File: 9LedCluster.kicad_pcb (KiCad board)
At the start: 4 copper layers, 26 x 26 mm, 43 parts, among them J1 Input, J2 Output, U1 LMR54406DBVR, U2 TLC5971RGE

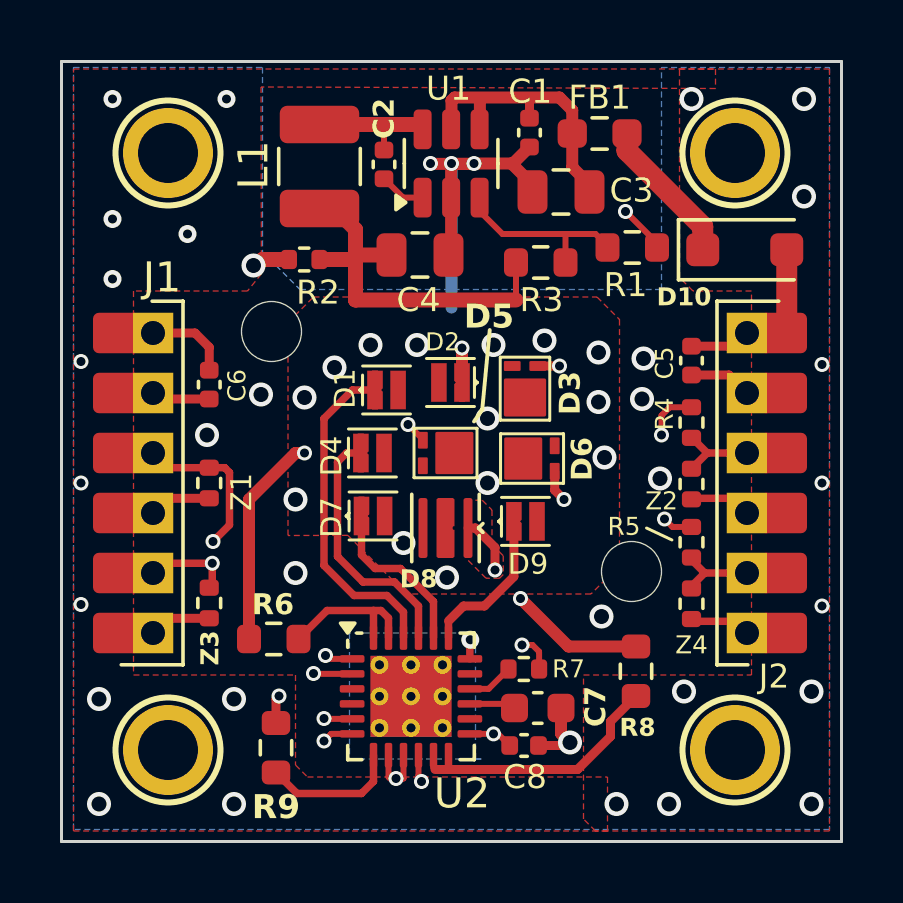
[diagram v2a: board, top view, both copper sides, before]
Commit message: Fix center ref for CREE LEDs for 9LED.
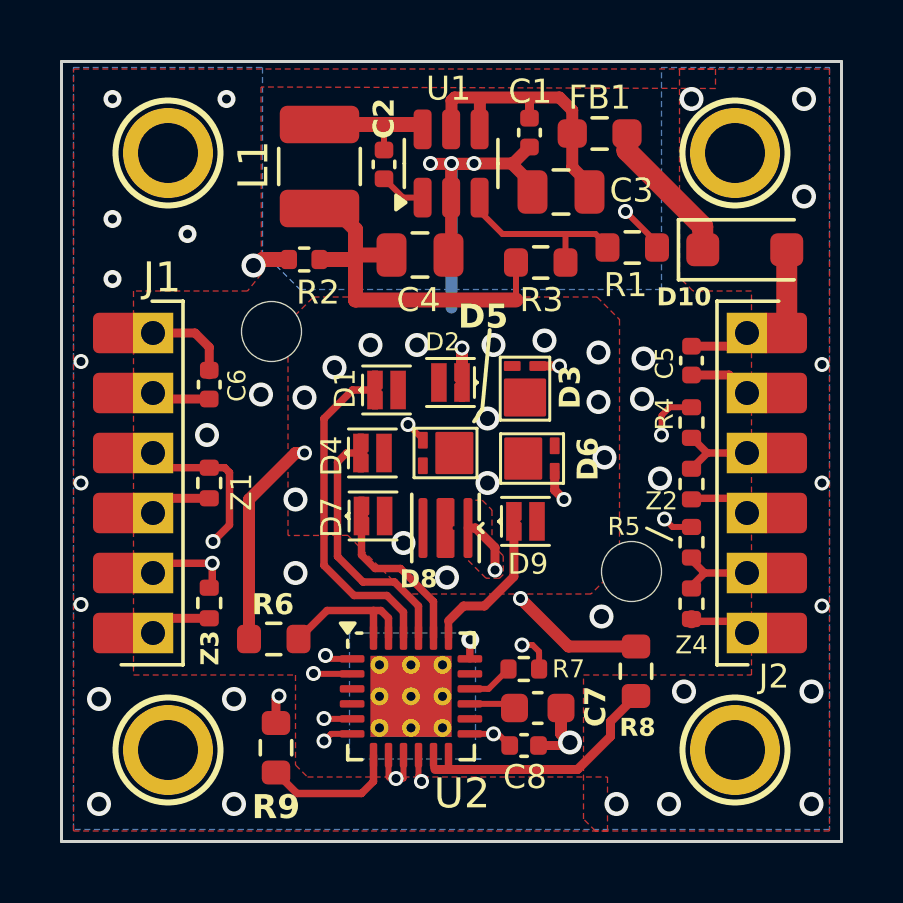
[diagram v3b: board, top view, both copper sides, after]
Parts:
- added FID1: Fiducial_0402_Pad, NwcPcbLibrary:Fiducial_0402_Pad, F.Cu at (121.0, 118.6)
- added FID2: Fiducial_0402_Pad, NwcPcbLibrary:Fiducial_0402_Pad, F.Cu at (104.9, 110.3)
- moved D3 0.20 mm to (115.5, 110.9)
- moved D6 0.20 mm to (115.7, 113.2)
- moved D5 0.19 mm to (112.8, 113.0)
